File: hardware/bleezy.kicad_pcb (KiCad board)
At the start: 2 copper layers, 65 x 30 mm, 33 parts, among them IC1 NRF51822, P1 Analog Header, P2 Digital Con 2, P3 Raspberry_Pi_+_Conn, P4 Digital Con 1, P5 Power Con, P6 TST, Q1 BSS138, U1 LD3985M33R, U5 DMMT5401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

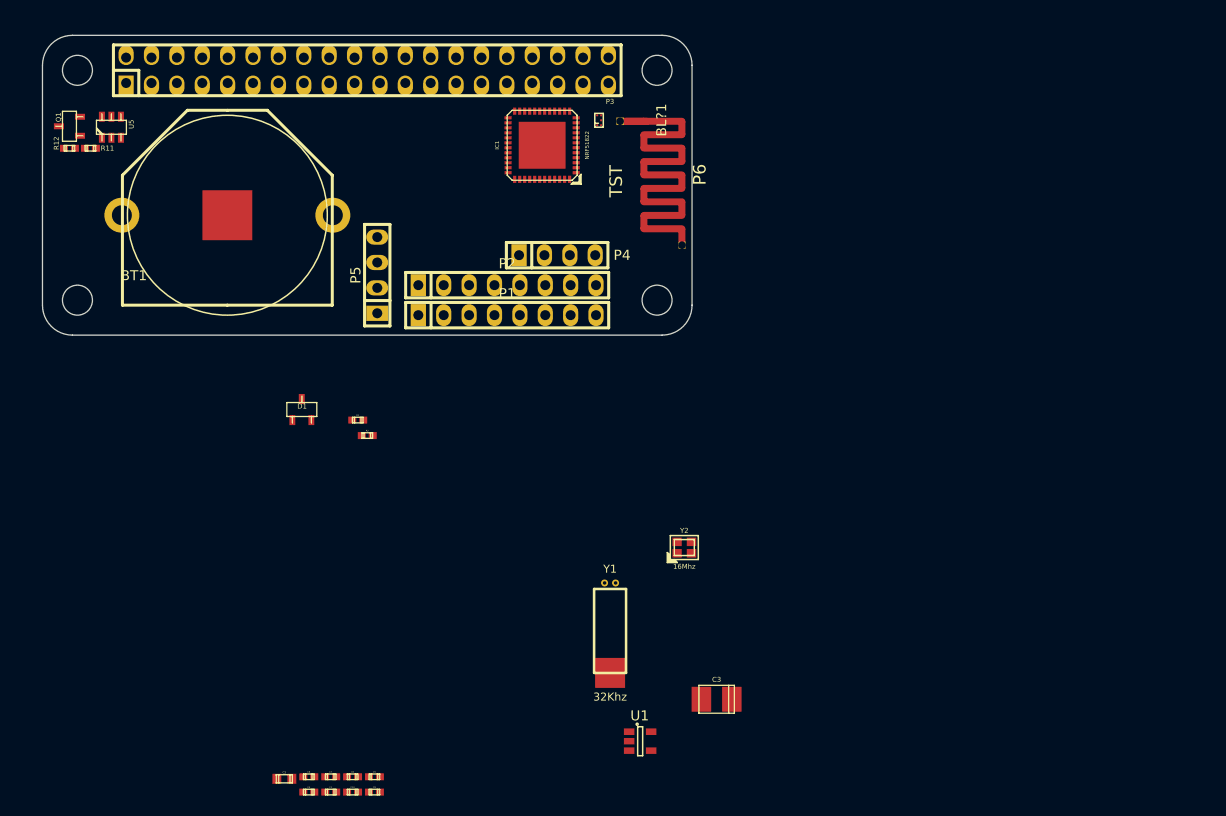
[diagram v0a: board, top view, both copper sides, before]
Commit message: redid basic layout, some routing
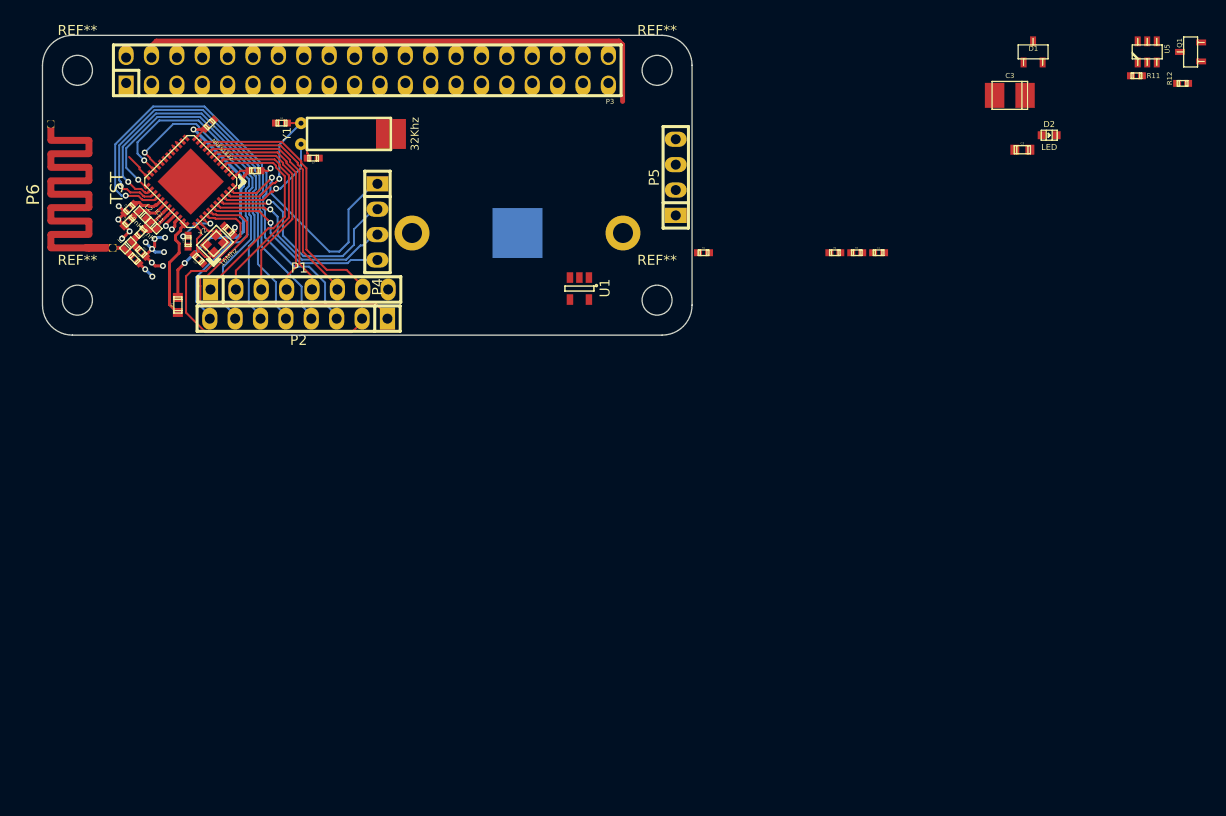
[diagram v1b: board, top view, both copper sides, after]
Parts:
- removed BL?1: nRF5x_BALUN, openfet-footprint:BALUN_5BGA_ST
- added C11: 2.2pf, w_smd_cap:c_0402, F.Cu at (47.9, 59.4)
- added C12: 1pf, w_smd_cap:c_0402, F.Cu at (48.0, 61.4)
- added C13: 1.5pf, w_smd_cap:c_0402, F.Cu at (47.3, 62.1)
- added C14: 100nf, w_smd_cap:c_0402, F.Cu at (54.8, 48.6)
- added C15: 100nf, w_smd_cap:c_0402, F.Cu at (59.4, 53.2)
- added D2: LED, w_smd_leds:Led_0603, F.Cu at (138.8, 49.7)
- added JP1: JUMPER, w_smd_cap:c_0603, F.Cu at (51.6, 66.7)
- added L1: 4.7nH, w_smd_inductors:inductor_smd_0402, F.Cu at (49.2, 58.8)
- added L2: 10nH, w_smd_inductors:inductor_smd_0402, F.Cu at (48.1, 57.6)
- added L3: 3.3nH, w_smd_inductors:inductor_smd_0402, F.Cu at (46.7, 60.7)
- added R3: R, w_smd_resistors:r_0402, F.Cu at (119.6, 61.5)
- BT1: moved to B.Cu
- moved Q1 112.4 mm to (153.0, 41.4)
- moved R12 111.6 mm to (152.2, 44.5)
- moved R11 104.9 mm to (147.6, 43.7)
- moved U5 103.9 mm to (148.6, 41.4)
- moved C2 97.0 mm to (136.2, 51.1)
- moved D1 81.5 mm to (137.2, 41.4)
- moved C1 76.9 mm to (121.8, 61.5)
- moved C3 67.2 mm to (134.9, 45.7)
- moved C4 67.0 mm to (62.0, 48.5)
- moved C7 61.9 mm to (65.2, 52.0), turned to 180 degrees
- moved C6 61.1 mm to (46.8, 57.0), turned to 45 degrees
- moved C8 58.4 mm to (46.7, 58.3), turned to 45 degrees
- moved C9 58.1 mm to (56.7, 59.2), turned to 135 degrees
- moved C5 56.7 mm to (52.7, 60.3), turned to 90 degrees
- moved Y1 56.0 mm to (68.4, 49.6), turned to 90 degrees
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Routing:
- net /Back Power Protection/5V_MCU: track 0.00 -> 54.3 mm
- net Net-(IC1-Pad28): track 0.00 -> 47.7 mm, vias 0 -> 1
- net Net-(IC1-Pad27): track 0.00 -> 43.5 mm, vias 0 -> 1
- net Net-(IC1-Pad26): track 0.00 -> 40.1 mm, vias 0 -> 1
- net Net-(IC1-Pad25): track 0.00 -> 36.9 mm, vias 0 -> 1
- net Net-(IC1-Pad40): track 0.00 -> 35.0 mm
- net Net-(IC1-Pad22): track 0.00 -> 34.4 mm, vias 0 -> 1
- net Net-(IC1-Pad41): track 0.00 -> 34.2 mm
- net Net-(IC1-Pad21): track 0.00 -> 33.3 mm, vias 0 -> 1
- net VCC: track 0.00 -> 29.4 mm, vias 0 -> 3
- net Net-(IC1-Pad10): track 0.00 -> 27.4 mm
- net Net-(IC1-Pad47): track 0.00 -> 24.4 mm, vias 0 -> 1
- net Net-(IC1-Pad9): track 0.00 -> 24.4 mm
- net Net-(IC1-Pad8): track 0.00 -> 22.5 mm
- net Net-(IC1-Pad44): track 0.00 -> 22.4 mm, vias 0 -> 1
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
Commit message: finished routing
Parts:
- removed P4: Digital Con 1, w_pin_strip:pin_strip_4
- added G***: LOGO, project_footprints:BLEezy_logo, F.Cu at (89.9, 57.5)
- moved D2 94.2 mm to (46.6, 68.7), turned to 180 degrees
- moved Q1 73.0 mm to (84.3, 66.1), turned to 0 degrees
- moved R3 70.9 mm to (49.1, 68.7), turned to 180 degrees
- moved R12 68.2 mm to (86.5, 62.9), turned to 90 degrees
- moved R11 67.9 mm to (81.9, 61.0), turned to 270 degrees
- moved U5 67.7 mm to (84.3, 62.5), turned to 180 degrees
- moved D1 60.9 mm to (79.6, 61.1)
- moved C2 58.8 mm to (79.6, 67.2)
- moved C3 56.3 mm to (79.6, 56.3), turned to 90 degrees
- moved R2 40.8 mm to (77.0, 67.3), turned to 180 degrees
- moved C1 39.9 mm to (81.9, 63.5), turned to 270 degrees
- moved R1 27.2 mm to (77.3, 65.4), turned to 270 degrees
- moved U1 12.2 mm to (79.6, 64.7)
- moved P5 0.59 mm to (101.5, 54.5)
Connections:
- IC1 pad 49: Net-(IC1-Pad49) -> GND
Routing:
- net GND: track 19.2 -> 217.4 mm, vias 17 -> 42
- net VCC: track 29.4 -> 100.6 mm, vias 3 -> 7
- net +5V: track 0.00 -> 56.3 mm, vias 0 -> 2
- net /PI_SPI_CE0: track 0.00 -> 41.8 mm
- net /PI_GPIO6: track 0.00 -> 39.1 mm, vias 0 -> 1
- net /PI_SPI_SCLK: track 0.00 -> 37.6 mm, vias 0 -> 1
- net /nRF_SWDCLK: track 2.75 -> 38.2 mm
- net /nRF_SWDIO: track 0.00 -> 35.4 mm, vias 0 -> 1
- net /Back Power Protection/5V_MCU: track 54.3 -> 89.5 mm, vias 0 -> 2
- net Net-(BT1-Pad1): track 0.00 -> 34.0 mm, vias 0 -> 1
- net /PI_SPI_MISO: track 0.00 -> 34.0 mm, vias 0 -> 1
- net /PI_GPIO5: track 0.00 -> 33.7 mm, vias 0 -> 2
- net /VSense: track 0.00 -> 33.3 mm, vias 0 -> 2
- net Net-(D2-Pad2): track 0.00 -> 32.0 mm, vias 0 -> 4
- net /PI_SPI_MOSI: track 0.00 -> 27.7 mm, vias 0 -> 1
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- added copper zone on B.Cu, net GND
- added copper zone on F.Cu, net GND
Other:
- board text added: "5V VCC GND GND"
- board text added: "CERN OHL V1.2"
- board text added: "Julien Marcus & OpenFET"
- board text added: "P0.00 P0.01 P0.02 P0.03 P0.04 P0.05 P0.06 GND"
- board text added: "P0.15 P0.16 P0.17 P0.18 P0.19 P0.20 P0.21 P0.22"
- board text added: "P1"
- board text added: "P2"
- board text added: "PI Connections GPIO14>P09 GPIO15>P10 GPIO10>P11 GPIO09>P12 GPIO11>P13 GPIO08>P14 GPIO05>P07 GPIO06>P08"

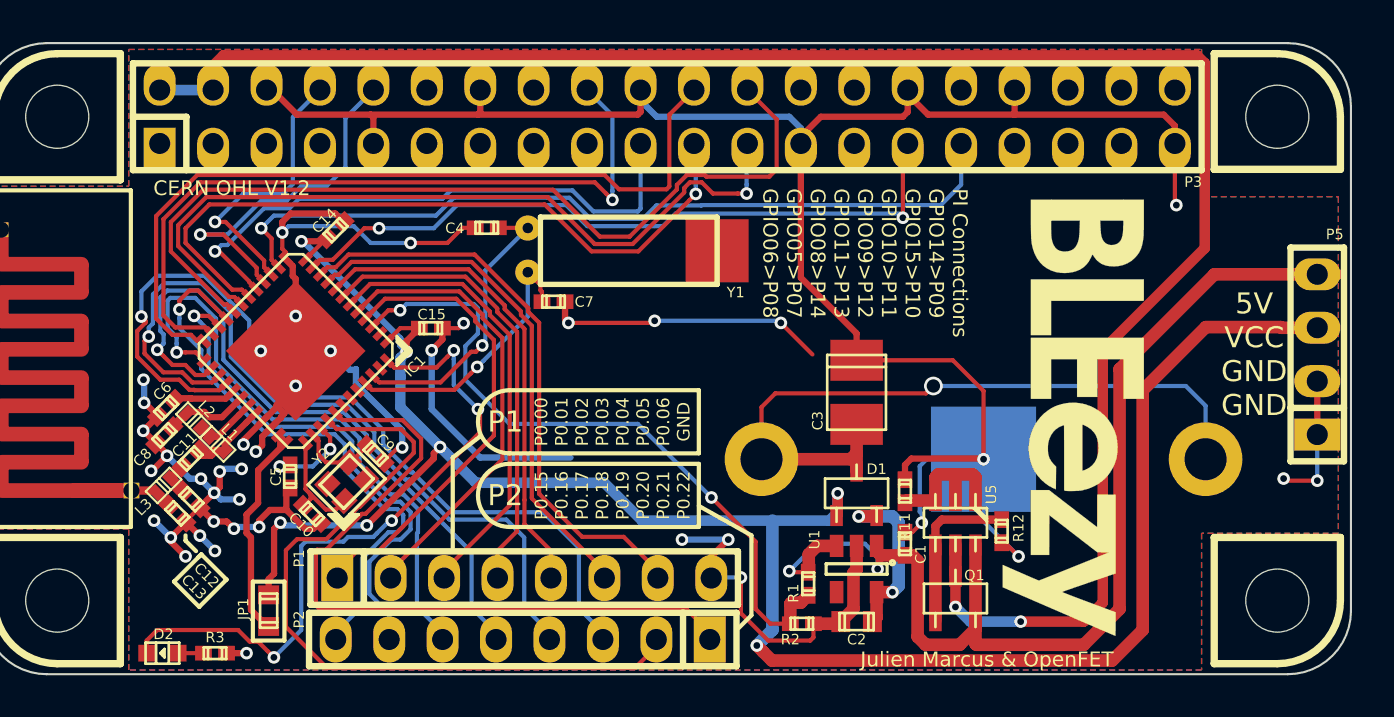
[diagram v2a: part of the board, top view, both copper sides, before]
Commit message: rerouted with new pinout and bat on top
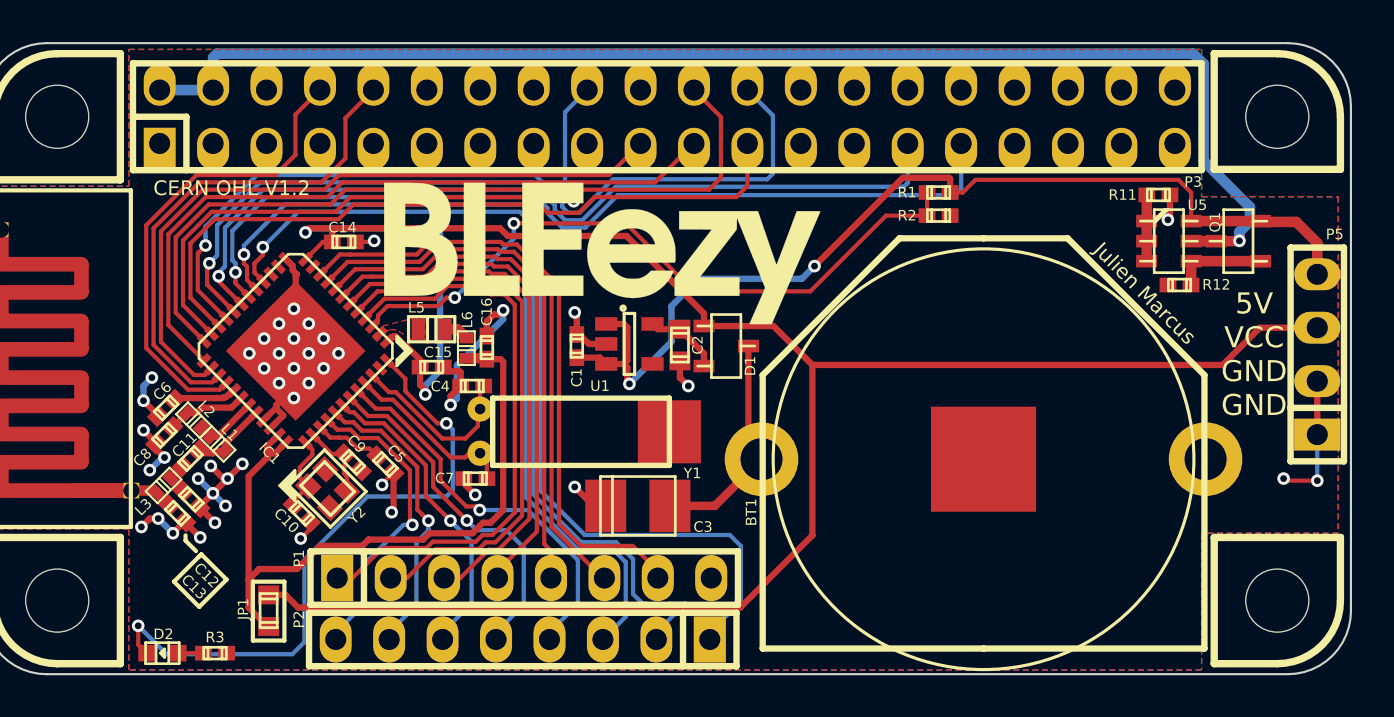
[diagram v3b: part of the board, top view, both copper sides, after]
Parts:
- added C16: 1.0uf, w_smd_cap:c_0402, F.Cu at (62.0, 54.2)
- added L5: 10uH, w_smd_inductors:inductor_smd_0603, F.Cu at (59.4, 53.3)
- added L6: 15nH, w_smd_inductors:inductor_smd_0402, F.Cu at (61.0, 54.2)
- BT1: moved to F.Cu
- moved G*** 23.7 mm to (67.5, 49.7), turned to 0 degrees
- moved Q1 21.7 mm to (97.7, 49.1), turned to 90 degrees
- moved R2 20.5 mm to (83.5, 47.9)
- moved R1 19.6 mm to (83.5, 46.8), turned to 180 degrees
- moved R11 18.5 mm to (93.9, 46.9), turned to 180 degrees
- moved C1 18.2 mm to (66.3, 54.1)
- moved U5 16.8 mm to (94.4, 49.1), turned to 270 degrees
- moved C2 15.6 mm to (71.2, 54.1), turned to 90 degrees
- moved U1 15.2 mm to (68.8, 54.0), turned to 0 degrees
- moved R12 14.4 mm to (95.0, 51.2), turned to 0 degrees
- moved C3 11.7 mm to (69.2, 61.7), turned to 180 degrees
- moved D1 9.35 mm to (73.4, 54.1), turned to 270 degrees
- moved C7 9.19 mm to (61.5, 60.4), turned to 0 degrees
- moved Y1 8.90 mm to (66.1, 58.2)
- moved C4 7.55 mm to (61.3, 56.0)
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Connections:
- net Net-(IC1-Pad10) renamed /P0.06
- net Net-(IC1-Pad4) renamed /P0.00
- net Net-(IC1-Pad5) renamed /P0.01
- net Net-(IC1-Pad6) renamed /P0.02
- net Net-(IC1-Pad7) renamed /P0.03
- net Net-(IC1-Pad8) renamed /P0.04
- net Net-(IC1-Pad9) renamed /P0.05
- IC1 pad 11: /PI_GPIO5 -> Net-(IC1-Pad11)
- IC1 pad 14: /PI_GPIO6 -> Net-(IC1-Pad14)
- IC1 pad 15: /PI_TXD -> Net-(IC1-Pad15)
- IC1 pad 16: /PI_RXD -> /P0.12
- IC1 pad 17: /PI_SPI_MOSI -> /P0.11
- IC1 pad 18: /PI_SPI_MISO -> /P0.13
- IC1 pad 19: /PI_SPI_SCLK -> /PI_GPIO6
- IC1 pad 20: /PI_SPI_CE0 -> /PI_GPIO5
- IC1 pad 21: Net-(IC1-Pad21) -> /PI_SPI_CE0
- IC1 pad 22: Net-(IC1-Pad22) -> /PI_SPI_SCLK
- IC1 pad 25: Net-(IC1-Pad25) -> /PI_SPI_MISO
- IC1 pad 26: Net-(IC1-Pad26) -> /PI_SPI_MOSI
- IC1 pad 27: Net-(IC1-Pad27) -> /PI_RXD
- IC1 pad 28: Net-(IC1-Pad28) -> /PI_TXD
- IC1 pad 40: Net-(IC1-Pad40) -> /P0.21
- IC1 pad 41: Net-(IC1-Pad41) -> /P0.22
- IC1 pad 42: Net-(IC1-Pad42) -> /P0.23
- IC1 pad 43: Net-(IC1-Pad43) -> /P0.24
- IC1 pad 44: Net-(IC1-Pad44) -> /P0.25
- P2 pad 1: Net-(IC1-Pad41) -> /P0.13
- P2 pad 2: Net-(IC1-Pad40) -> /P0.11
- P2 pad 3: Net-(IC1-Pad28) -> /P0.12
- P2 pad 4: Net-(IC1-Pad27) -> /P0.25
- P2 pad 5: Net-(IC1-Pad26) -> /P0.24
- P2 pad 6: Net-(IC1-Pad25) -> /P0.23
- P2 pad 7: Net-(IC1-Pad22) -> /P0.22
- P2 pad 8: Net-(IC1-Pad21) -> /P0.21
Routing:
- net GND: track 217.4 -> 71.5 mm, vias 42 -> 45
- net /P0.13: track 0.00 -> 48.0 mm, vias 0 -> 1
- net /P0.11: track 0.00 -> 43.1 mm, vias 0 -> 1
- net Net-(IC1-Pad28): track 41.1 -> 0.00 mm, vias 1 -> 0
- net /P0.12: track 0.00 -> 38.7 mm, vias 0 -> 1
- net Net-(IC1-Pad27): track 37.1 -> 0.00 mm, vias 1 -> 0
- net Net-(IC1-Pad40): track 35.8 -> 0.00 mm
- net Net-(IC1-Pad41): track 34.5 -> 0.00 mm
- net Net-(IC1-Pad26): track 32.3 -> 0.00 mm, vias 1 -> 0
- net Net-(IC1-Pad25): track 28.9 -> 0.00 mm, vias 1 -> 0
- net Net-(IC1-Pad21): track 27.3 -> 0.00 mm, vias 1 -> 0
- net /Back Power Protection/5V_MCU: track 89.5 -> 63.3 mm, vias 2 -> 1
- net Net-(IC1-Pad22): track 24.8 -> 0.00 mm, vias 1 -> 0
- net AVDD: track 10.6 -> 33.8 mm
- net Net-(BT1-Pad1): track 34.0 -> 10.9 mm, vias 1 -> 0
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- added copper zone on F.Cu, net Net-(IC1-Pad2)
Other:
- board text added: "Julien Marcus"
- board text removed: "Julien Marcus & OpenFET"

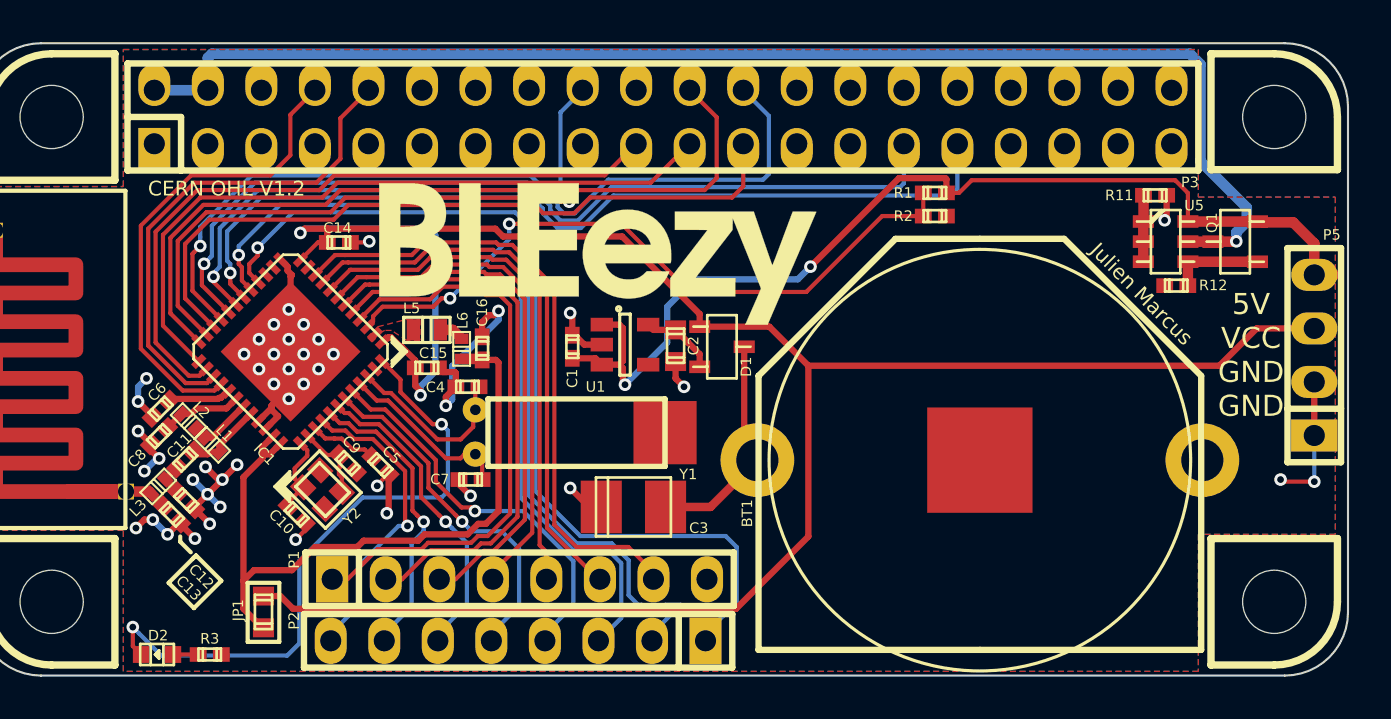
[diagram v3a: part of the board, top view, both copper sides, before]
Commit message: Updated PCB routing
Mostly aesthetic changes...
Beefed up a few power-lines.
Added guard-rings around the crystals
Made the B.Cu ground-plane contigous (although it has a narrow passage)
Removed a lot of unncessary vias
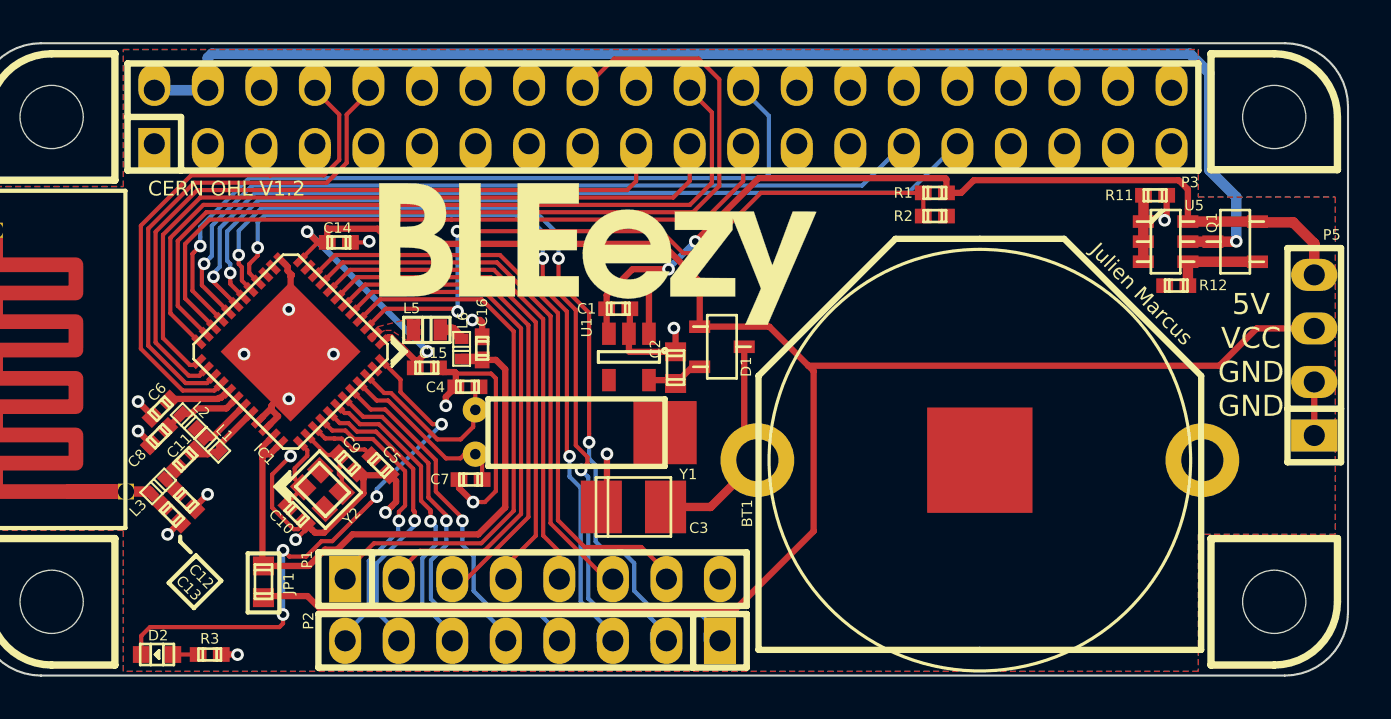
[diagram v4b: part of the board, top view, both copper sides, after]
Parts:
- moved C1 2.83 mm to (68.5, 52.3), turned to 180 degrees
- moved JP1 1.43 mm to (51.6, 65.3), turned to 270 degrees
- moved C2 1.04 mm to (71.2, 55.1), turned to 270 degrees
- moved P2 0.69 mm to (64.4, 68.0)
- moved P1 0.62 mm to (64.4, 65.1)
- moved U1 0.61 mm to (69.0, 54.6), turned to 270 degrees
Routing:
- net /nRF_SWDIO: track 30.4 -> 44.3 mm, vias 1 -> 0
- net VCC: track 108.3 -> 102.5 mm
- net AVDD: track 33.8 -> 29.2 mm
- net Net-(D2-Pad2): track 30.2 -> 26.2 mm, vias 2 -> 4
- net +5V: track 49.4 -> 45.8 mm
- net /P0.13: track 48.0 -> 44.9 mm, vias 1 -> 3
- net GND: track 71.5 -> 74.3 mm, vias 45 -> 19
- net /PI_GPIO5: track 42.0 -> 39.3 mm
- net /PI_TXD: track 22.6 -> 25.1 mm
- net /PI_GPIO6: track 43.7 -> 41.3 mm
- net /PI_SPI_CE0: track 39.2 -> 37.6 mm
- net /PI_SPI_MISO: track 33.5 -> 35.0 mm
- net /P0.25: track 18.8 -> 17.5 mm
- net /P0.11: track 43.1 -> 42.0 mm, vias 1 -> 3
- net /P0.00: track 27.8 -> 26.7 mm
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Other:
- net class Default: via_dia 0.889 -> 0.6; via_drill 0.635 -> 0.32
